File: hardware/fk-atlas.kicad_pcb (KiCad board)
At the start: 2 copper layers, 88.4 x 80.3 mm, 128 parts, among them J1 CONN-HDR-2x5, J2 MICRO-USB, J201 CONN_01X02, J3 Conn_01x02, J301 CONN_01X02, J4 Conn_01x09, J401 CONN_01X02, J501 CONN_01X02, J601 CONN_01X02, P2 ATLAS_EC_PROBE, P3 ATLAS_RTD_PROBE, P4 ATLAS_PH_PROBE, P5 ATLAS_DO_PROBE, P6 ATLAS_ORP_PROBE, Q1 2N7002LT1G, Q2 2N7002LT1G, Q3 2N7002LT1G, Q4 2N7002LT1G, Q5 2N7002LT1G, SW1 SPNO, U1 S25FL1xxK0XM, U2 ATSAMD21G18A-AU, U201 ADM3260, U202 ATLAS_EC, U3 MCP1700T-3302E/MB, U301 ADM3260, U302 ATLAS_RTD, U401 ADM3260, U402 ATLAS_PH, U501 ADM3260, U502 ATLAS_DO, U601 ADM3260, U602 ATLAS_ORP, Y1 FC-135

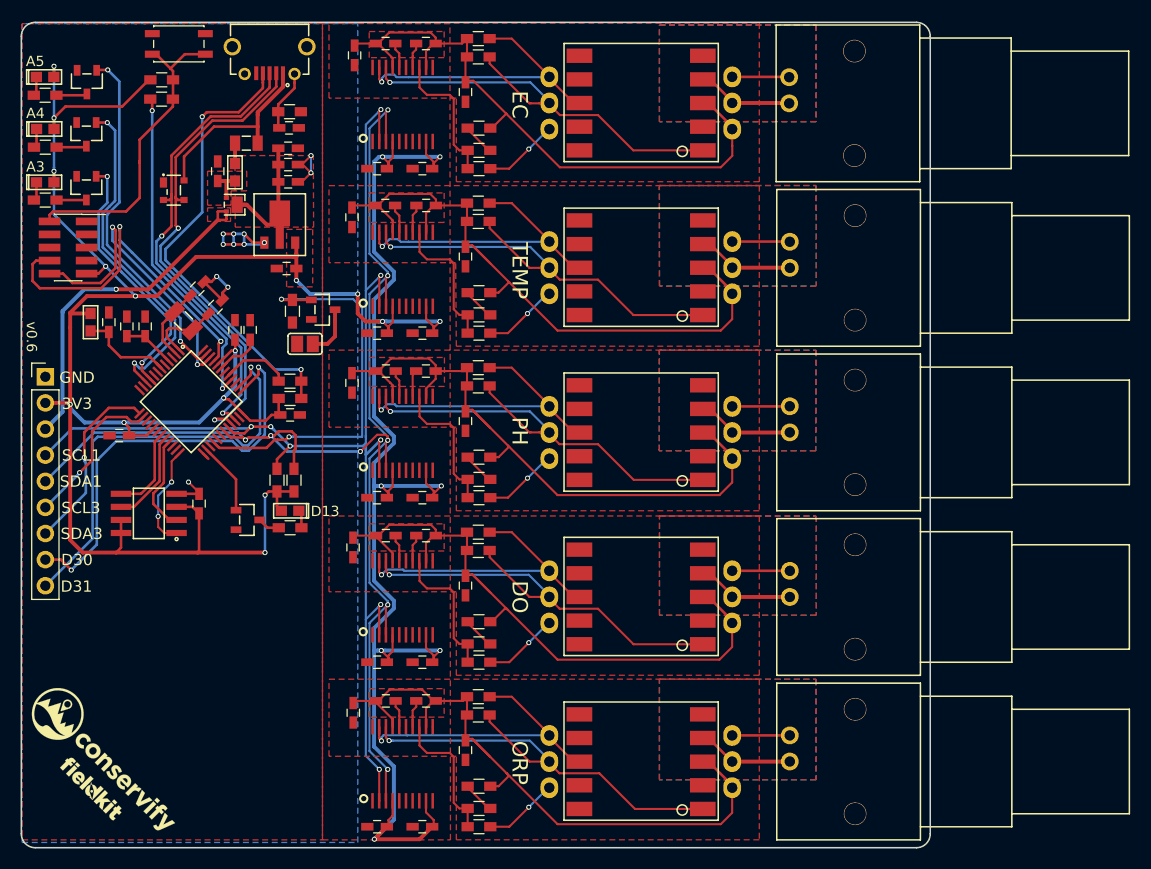
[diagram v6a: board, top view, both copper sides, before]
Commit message: Adding mounting holes for Atlas.
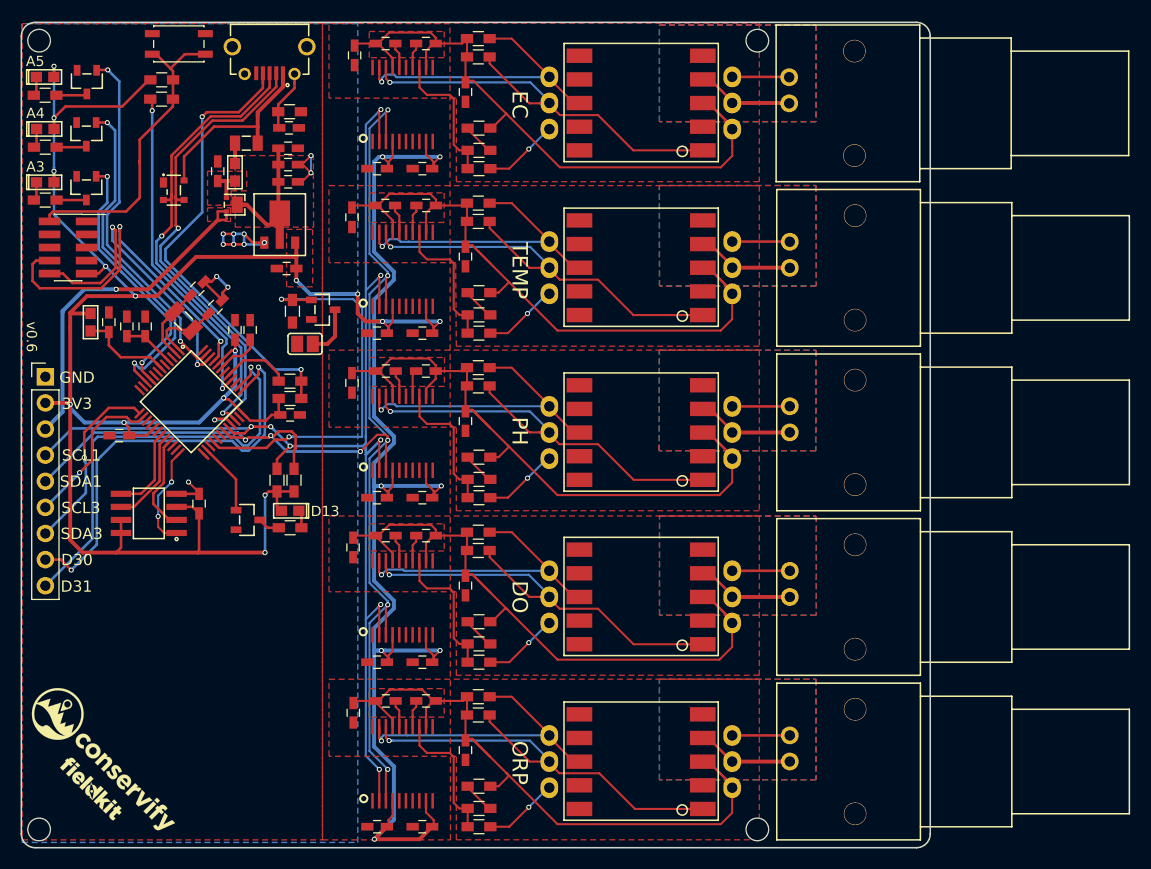
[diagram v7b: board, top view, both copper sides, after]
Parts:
- added M1: MOUNT_HOLE, RocketScreamKicadLibrary:HOLE_NPTH_2.2MM, F.Cu at (117.5, 135.9)
- added M2: MOUNT_HOLE, RocketScreamKicadLibrary:HOLE_NPTH_2.2MM, F.Cu at (117.5, 59.2)
- added M3: MOUNT_HOLE, RocketScreamKicadLibrary:HOLE_NPTH_2.2MM, F.Cu at (187.3, 135.9)
- added M4: MOUNT_HOLE, RocketScreamKicadLibrary:HOLE_NPTH_2.2MM, F.Cu at (187.3, 59.2)
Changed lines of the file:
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@@
     (tracks 1242)
     (zones 0)
-    (modules 128)
+    (modules 132)
     (nets 117)
   )
@@
       (net 101 "Net-(D4-Pad1)"))
   )
+  (module RocketScreamKicadLibrary:HOLE_NPTH_2.2MM (layer F.Cu)
+    (at 117.475 135.89)
+    (fp_text reference M1 (at 0 -3.175) (layer F.SilkS) hide
+      (effects (font (size 1 1) (thickness 0.15)))
+    )
+    (fp_text value MOUNT_HOLE (at 0 3.175) (layer F.Fab)
+      (effects (font (size 1 1) (thickness 0.15)))
+    )
+    (pad "" np_thru_hole circle (at 0 0) (size 2.2 2.2) (drill 2.2) (layers *.Cu *.Mask F.SilkS))
+  )
+  (module RocketScreamKicadLibrary:HOLE_NPTH_2.2MM (layer F.Cu)
+    (at 117.475 59.182)
+    (fp_text reference M2 (at 0 -3.175) (layer F.SilkS) hide
+      (effects (font (size 1 1) (thickness 0.15)))
+    )
+    (fp_text value MOUNT_HOLE (at 0 3.175) (layer F.Fab)
+      (effects (font (size 1 1) (thickness 0.15)))
+    )
+    (pad "" np_thru_hole circle (at 0 0) (size 2.2 2.2) (drill 2.2) (layers *.Cu *.Mask F.SilkS))
+  )
+  (module RocketScreamKicadLibrary:HOLE_NPTH_2.2MM (layer F.Cu)
+    (at 187.325 135.89)
+    (fp_text reference M3 (at 0 -3.175) (layer F.SilkS) hide
+      (effects (font (size 1 1) (thickness 0.15)))
+    )
+    (fp_text value MOUNT_HOLE (at 0 3.175) (layer F.Fab)
+      (effects (font (size 1 1) (thickness 0.15)))
+    )
+    (pad "" np_thru_hole circle (at 0 0) (size 2.2 2.2) (drill 2.2) (layers *.Cu *.Mask F.SilkS))
+  )
+  (module RocketScreamKicadLibrary:HOLE_NPTH_2.2MM (layer F.Cu)
+    (at 187.325 59.182)
+    (fp_text reference M4 (at 0 -3.175) (layer F.SilkS) hide
+      (effects (font (size 1 1) (thickness 0.15)))
+    )
+    (fp_text value MOUNT_HOLE (at 0 3.175) (layer F.Fab)
+      (effects (font (size 1 1) (thickness 0.15)))
+    )
+    (pad "" np_thru_hole circle (at 0 0) (size 2.2 2.2) (drill 2.2) (layers *.Cu *.Mask F.SilkS))
+  )
   (gr_text D13 (at 145.288 104.9528) (layer F.SilkS)
     (effects (font (size 1 1) (thickness 0.2)))
@@
     (connect_pads (clearance 0.2032))
     (min_thickness 0.2032)
-    (fill yes (arc_segments 32) (thermal_gap 0.254) (thermal_bridge_width 0.254))
+    (fill (arc_segments 32) (thermal_gap 0.254) (thermal_bridge_width 0.254))
     (polygon
       (pts
@@
     (connect_pads (clearance 0.2032))
     (min_thickness 0.2032)
-    (fill yes (arc_segments 32) (thermal_gap 0.254) (thermal_bridge_width 0.254))
+    (fill (arc_segments 32) (thermal_gap 0.254) (thermal_bridge_width 0.254))
     (polygon
       (pts
@@
     (connect_pads (clearance 0.2032))
     (min_thickness 0.2032)
-    (fill yes (arc_segments 32) (thermal_gap 0.254) (thermal_bridge_width 0.254))
+    (fill (arc_segments 32) (thermal_gap 0.254) (thermal_bridge_width 0.254))
     (polygon
       (pts
@@
     (connect_pads (clearance 0.2032))
     (min_thickness 0.2032)
-    (fill yes (arc_segments 32) (thermal_gap 0.254) (thermal_bridge_width 0.254))
+    (fill (arc_segments 32) (thermal_gap 0.254) (thermal_bridge_width 0.254))
     (polygon
       (pts
@@
     (connect_pads (clearance 0.2032))
     (min_thickness 0.2032)
-    (fill yes (arc_segments 32) (thermal_gap 0.254) (thermal_bridge_width 0.254))
+    (fill (arc_segments 32) (thermal_gap 0.254) (thermal_bridge_width 0.254))
     (polygon
       (pts
@@
     (connect_pads (clearance 0.2032))
     (min_thickness 0.2032)
-    (fill yes (arc_segments 32) (thermal_gap 0.254) (thermal_bridge_width 0.254))
+    (fill (arc_segments 32) (thermal_gap 0.254) (thermal_bridge_width 0.254))
     (polygon
       (pts
@@
     (connect_pads (clearance 0.2032))
     (min_thickness 0.254)
-    (fill yes (arc_segments 16) (thermal_gap 0.508) (thermal_bridge_width 0.508))
+    (fill (arc_segments 16) (thermal_gap 0.508) (thermal_bridge_width 0.508))
     (polygon
       (pts
@@
     (connect_pads (clearance 0.2032))
     (min_thickness 0.253)
-    (fill yes (arc_segments 32) (thermal_gap 0.254) (thermal_bridge_width 0.254))
+    (fill (arc_segments 32) (thermal_gap 0.254) (thermal_bridge_width 0.254))
     (polygon
       (pts
@@
     (connect_pads (clearance 0.2032))
     (min_thickness 0.254)
-    (fill yes (arc_segments 16) (thermal_gap 0.508) (thermal_bridge_width 0.508))
+    (fill (arc_segments 16) (thermal_gap 0.508) (thermal_bridge_width 0.508))
     (polygon
       (pts
@@
     (connect_pads (clearance 0.2032))
     (min_thickness 0.254)
-    (fill yes (arc_segments 16) (thermal_gap 0.508) (thermal_bridge_width 0.508))
+    (fill (arc_segments 16) (thermal_gap 0.508) (thermal_bridge_width 0.508))
     (polygon
       (pts
@@
     (connect_pads (clearance 0.2032))
     (min_thickness 0.254)
-    (fill yes (arc_segments 16) (thermal_gap 0.508) (thermal_bridge_width 0.508))
+    (fill (arc_segments 16) (thermal_gap 0.508) (thermal_bridge_width 0.508))
     (polygon
       (pts
@@
     (connect_pads (clearance 0.2032))
     (min_thickness 0.254)
-    (fill yes (arc_segments 16) (thermal_gap 0.508) (thermal_bridge_width 0.508))
+    (fill (arc_segments 16) (thermal_gap 0.508) (thermal_bridge_width 0.508))
     (polygon
       (pts
@@
     (connect_pads (clearance 0.2032))
     (min_thickness 0.254)
-    (fill yes (arc_segments 16) (thermal_gap 0.508) (thermal_bridge_width 0.508))
+    (fill (arc_segments 16) (thermal_gap 0.508) (thermal_bridge_width 0.508))
     (polygon
       (pts
@@
     (connect_pads (clearance 0.2032))
     (min_thickness 0.254)
-    (fill yes (arc_segments 16) (thermal_gap 0.508) (thermal_bridge_width 0.508))
+    (fill (arc_segments 16) (thermal_gap 0.508) (thermal_bridge_width 0.508))
     (polygon
       (pts
@@
     (connect_pads (clearance 0.2032))
     (min_thickness 0.254)
-    (fill yes (arc_segments 16) (thermal_gap 0.508) (thermal_bridge_width 0.508))
+    (fill (arc_segments 16) (thermal_gap 0.508) (thermal_bridge_width 0.508))
     (polygon
       (pts
@@
     (connect_pads (clearance 0.2032))
     (min_thickness 0.254)
-    (fill yes (arc_segments 16) (thermal_gap 0.508) (thermal_bridge_width 0.508))
+    (fill (arc_segments 16) (thermal_gap 0.508) (thermal_bridge_width 0.508))
     (polygon
       (pts
@@
     (connect_pads (clearance 0.2032))
     (min_thickness 0.254)
-    (fill yes (arc_segments 16) (thermal_gap 0.508) (thermal_bridge_width 0.508))
+    (fill (arc_segments 16) (thermal_gap 0.508) (thermal_bridge_width 0.508))
     (polygon
       (pts
@@
     (connect_pads (clearance 0.2032))
     (min_thickness 0.254)
-    (fill yes (arc_segments 16) (thermal_gap 0.508) (thermal_bridge_width 0.508))
+    (fill (arc_segments 16) (thermal_gap 0.508) (thermal_bridge_width 0.508))
     (polygon
       (pts
@@
     (connect_pads (clearance 0.2032))
     (min_thickness 0.254)
-    (fill yes (arc_segments 16) (thermal_gap 0.508) (thermal_bridge_width 0.508))
+    (fill (arc_segments 16) (thermal_gap 0.508) (thermal_bridge_width 0.508))
     (polygon
       (pts
@@
     (connect_pads (clearance 0.2032))
     (min_thickness 0.254)
-    (fill yes (arc_segments 16) (thermal_gap 0.508) (thermal_bridge_width 0.508))
+    (fill (arc_segments 16) (thermal_gap 0.508) (thermal_bridge_width 0.508))
     (polygon
       (pts
@@
     (connect_pads (clearance 0.2032))
     (min_thickness 0.254)
-    (fill yes (arc_segments 16) (thermal_gap 0.508) (thermal_bridge_width 0.508))
+    (fill (arc_segments 16) (thermal_gap 0.508) (thermal_bridge_width 0.508))
     (polygon
       (pts
@@
     (connect_pads (clearance 0.2032))
     (min_thickness 0.254)
-    (fill yes (arc_segments 16) (thermal_gap 0.508) (thermal_bridge_width 0.508))
+    (fill (arc_segments 16) (thermal_gap 0.508) (thermal_bridge_width 0.508))
     (polygon
       (pts
@@
     (connect_pads (clearance 0.2032))
     (min_thickness 0.254)
-    (fill yes (arc_segments 16) (thermal_gap 0.508) (thermal_bridge_width 0.508))
+    (fill (arc_segments 16) (thermal_gap 0.508) (thermal_bridge_width 0.508))
     (polygon
       (pts
@@
     (connect_pads (clearance 0.2032))
     (min_thickness 0.2032)
-    (fill yes (arc_segments 32) (thermal_gap 0.254) (thermal_bridge_width 0.254))
+    (fill (arc_segments 32) (thermal_gap 0.254) (thermal_bridge_width 0.254))
     (polygon
       (pts
@@
     (connect_pads (clearance 0.2032))
     (min_thickness 0.2032)
-    (fill yes (arc_segments 32) (thermal_gap 0.254) (thermal_bridge_width 0.254))
+    (fill (arc_segments 32) (thermal_gap 0.254) (thermal_bridge_width 0.254))
     (polygon
       (pts
@@
     (connect_pads (clearance 0.2032))
     (min_thickness 0.2032)
-    (fill yes (arc_segments 32) (thermal_gap 0.254) (thermal_bridge_width 0.254))
+    (fill (arc_segments 32) (thermal_gap 0.254) (thermal_bridge_width 0.254))
     (polygon
       (pts
@@
     (connect_pads (clearance 0.2032))
     (min_thickness 0.2032)
-    (fill yes (arc_segments 32) (thermal_gap 0.254) (thermal_bridge_width 0.254))
+    (fill (arc_segments 32) (thermal_gap 0.254) (thermal_bridge_width 0.254))
     (polygon
       (pts

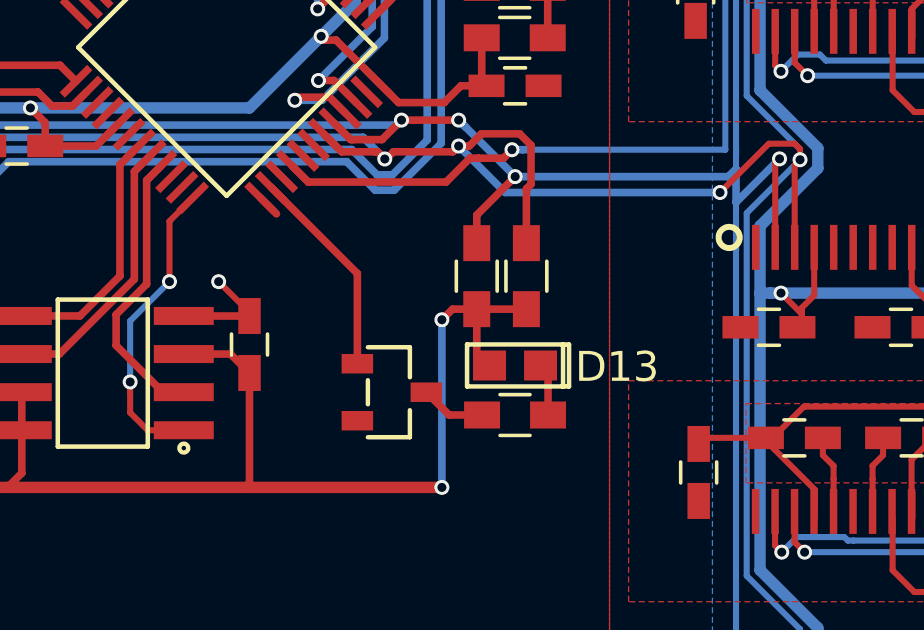
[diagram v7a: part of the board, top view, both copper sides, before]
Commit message: Flash memory is on PERIPH_GND now too.
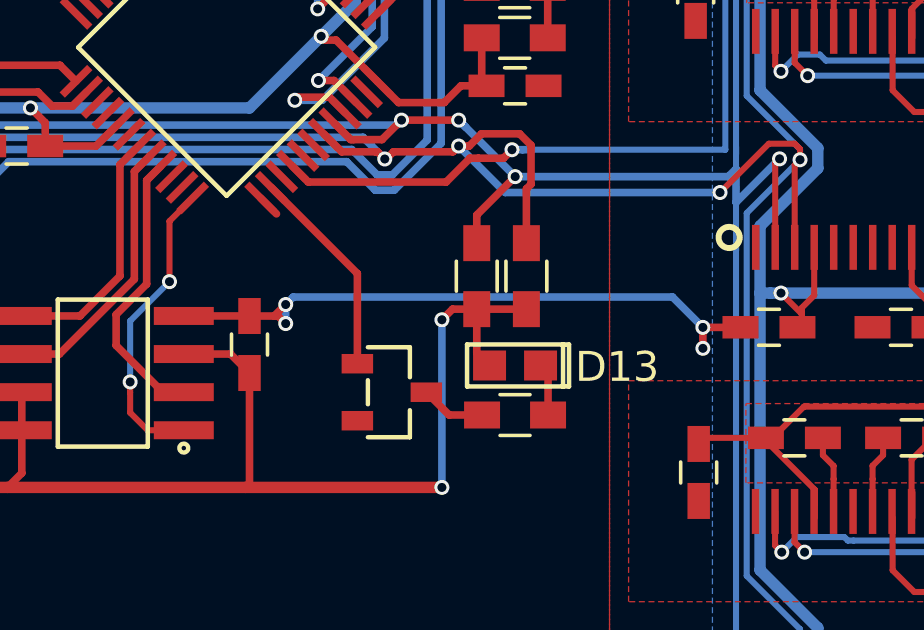
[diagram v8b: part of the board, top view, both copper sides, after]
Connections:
- net /ATLAS_EN renamed /PERIPH_EN
- C16 pad 2: GND -> /PERIPH_GND
- C201 pad 2: /ATLAS_GND -> /PERIPH_GND
- C202 pad 2: /ATLAS_GND -> /PERIPH_GND
- C301 pad 2: /ATLAS_GND -> /PERIPH_GND
- C302 pad 2: /ATLAS_GND -> /PERIPH_GND
- C401 pad 2: /ATLAS_GND -> /PERIPH_GND
- C402 pad 2: /ATLAS_GND -> /PERIPH_GND
- C501 pad 2: /ATLAS_GND -> /PERIPH_GND
- C502 pad 2: /ATLAS_GND -> /PERIPH_GND
- C601 pad 2: /ATLAS_GND -> /PERIPH_GND
- C602 pad 2: /ATLAS_GND -> /PERIPH_GND
- J3 pad 2: /ATLAS_GND -> /PERIPH_GND
- Q5 pad 3: /ATLAS_GND -> /PERIPH_GND
- U1 pad 4: GND -> /PERIPH_GND
- U201 pad 1: /ATLAS_GND -> /PERIPH_GND
- U201 pad 10: /ATLAS_GND -> /PERIPH_GND
- U201 pad 5: /ATLAS_GND -> /PERIPH_GND
- U201 pad 7: /ATLAS_GND -> /PERIPH_GND
- U201 pad 8: /ATLAS_GND -> /PERIPH_GND
- U301 pad 1: /ATLAS_GND -> /PERIPH_GND
- U301 pad 10: /ATLAS_GND -> /PERIPH_GND
- U301 pad 5: /ATLAS_GND -> /PERIPH_GND
- U301 pad 7: /ATLAS_GND -> /PERIPH_GND
- U301 pad 8: /ATLAS_GND -> /PERIPH_GND
- U401 pad 1: /ATLAS_GND -> /PERIPH_GND
- U401 pad 10: /ATLAS_GND -> /PERIPH_GND
- U401 pad 5: /ATLAS_GND -> /PERIPH_GND
- U401 pad 7: /ATLAS_GND -> /PERIPH_GND
- U401 pad 8: /ATLAS_GND -> /PERIPH_GND
- U501 pad 1: /ATLAS_GND -> /PERIPH_GND
- U501 pad 10: /ATLAS_GND -> /PERIPH_GND
- U501 pad 5: /ATLAS_GND -> /PERIPH_GND
- U501 pad 7: /ATLAS_GND -> /PERIPH_GND
- U501 pad 8: /ATLAS_GND -> /PERIPH_GND
- U601 pad 1: /ATLAS_GND -> /PERIPH_GND
- U601 pad 10: /ATLAS_GND -> /PERIPH_GND
- U601 pad 5: /ATLAS_GND -> /PERIPH_GND
- U601 pad 7: /ATLAS_GND -> /PERIPH_GND
- U601 pad 8: /ATLAS_GND -> /PERIPH_GND
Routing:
- net /PERIPH_GND: track 0.00 -> 26.7 mm, vias 0 -> 4
- net /ATLAS_GND: track 5.50 -> 0.00 mm
- net GND: track 28.8 -> 25.0 mm, vias 12 -> 11
- added copper zone on F.Cu, net /PERIPH_GND
- removed copper zone on F.Cu, net /ATLAS_GND
